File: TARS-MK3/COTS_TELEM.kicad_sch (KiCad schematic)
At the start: 13 parts, among them U1 RFM69HCW, U2 74HC4050D, U3 AP2112K-3.3, X1 uFL/SMA

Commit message: minor cots telem fixups
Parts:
- removed JP1: Conn_01x05_Female, symbol Connector:Conn_01x05_Female
- removed JP3: Conn_01x09_Female, symbol Connector:Conn_01x09_Female
- removed R2, R3: 100K, symbol D24V50F5:R
- removed U1: RFM69HCW, RF_Module:HOPERF_RFM9XW_THT, symbol RF_Module:RFM69HCW
- added J?: Conn_01x05_Male, Connector_PinHeader_2.54mm:PinHeader_1x05_P2.54mm_Vertical, symbol Connector:Conn_01x05_Male
- added J?: Conn_01x08_Male, Connector_PinHeader_2.54mm:PinHeader_1x09_P2.54mm_Vertical, symbol Connector:Conn_01x08_Male
- added U?: RFM96W-433S2, symbol RF_Module:RFM96W-433S2
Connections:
- net +3V3: no longer C1.1
- net GND: now also J?.7 (Pin_7), U?.1 (GND), U?.10 (GND), U?.8 (GND)
- net at JP2.1 (Pin_1), X1.ANTENNA (ANT): now also U?.9 (ANT)
- new net: J?.3 (Pin_3), U?.11 (DIO3)
- new net: J?.4 (Pin_4), U?.12 (DIO4)
- new net: J?.1 (Pin_1), U?.15 (DIO1)
- new net: J?.2 (Pin_2), U?.16 (DIO2)
- new net: J?.5 (Pin_5), U?.7 (DIO5)
- new net 3V3: C1.1, J?.8 (Pin_8), U?.13 (3.3V)
- new net B2B_SPI_MISO: J?.4 (Pin_4), U?.2 (MISO)
- new net B2B_SPI_MOSI: J?.5 (Pin_5), U?.3 (MOSI)
- new net B2B_SPI_SCK: J?.6 (Pin_6), U?.4 (SCK)
- new net TELEM_CS: J?.3 (Pin_3), U?.5 (NSS)
- new net TELEM_IRQ: J?.2 (Pin_2), U?.14 (DIO0)
- new net TELEM_RST: J?.1 (Pin_1), U?.6 (RESET)
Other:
- note removed: "DIO0"
- note removed: "DIO1"
- note removed: "DIO2"
- note removed: "DIO3"
- note removed: "DIO4"
- note removed: "DIO5"
- note removed: "MISO_3V"
- note removed: "MISO_5V"
- moved on the sheet: C1, C2, C3, JP2, R1, U2, U3, X1

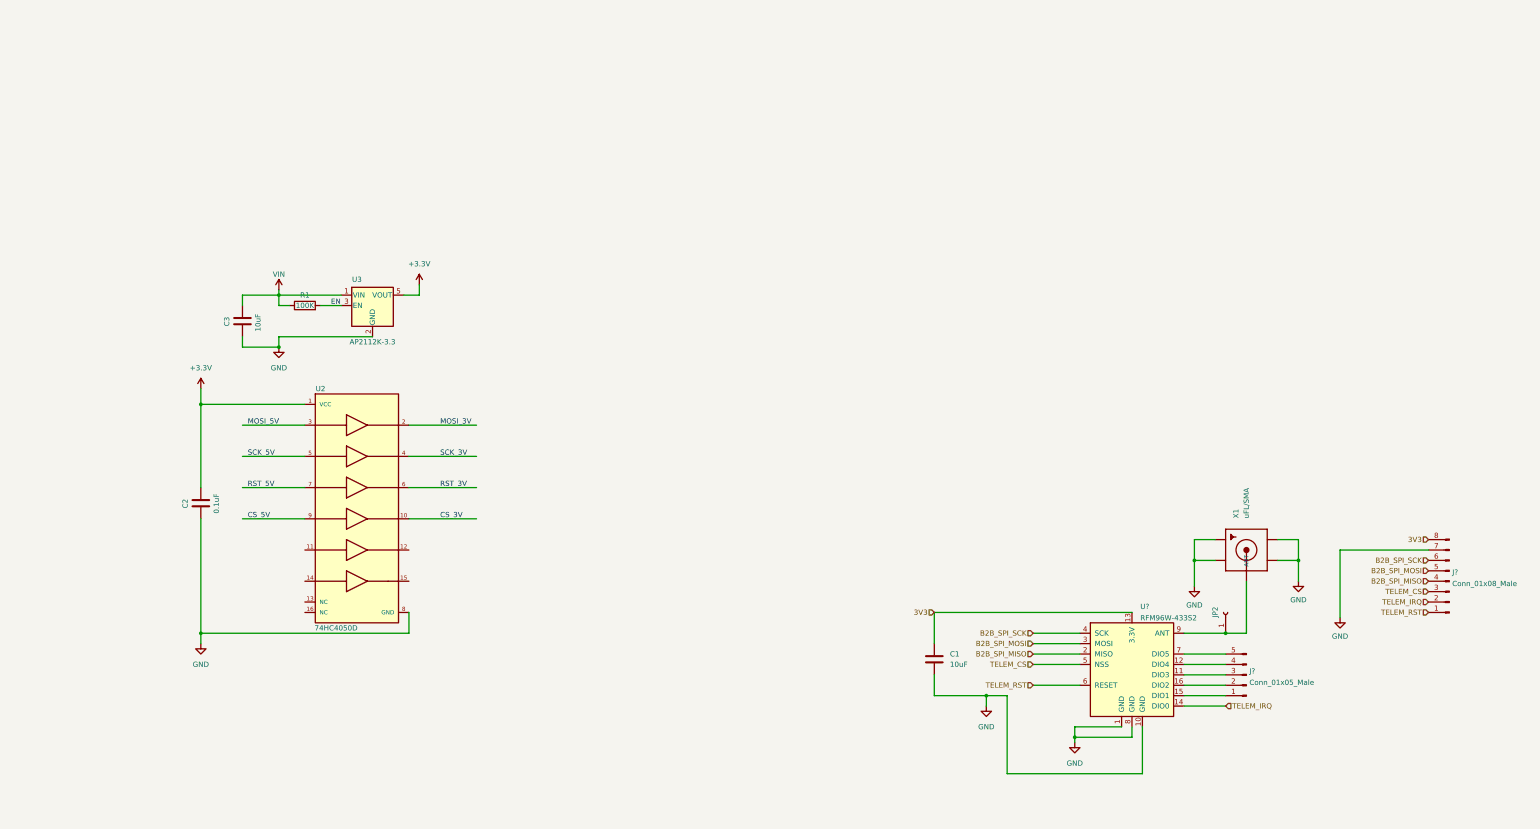
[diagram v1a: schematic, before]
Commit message: Applied template to COTS_TELEM
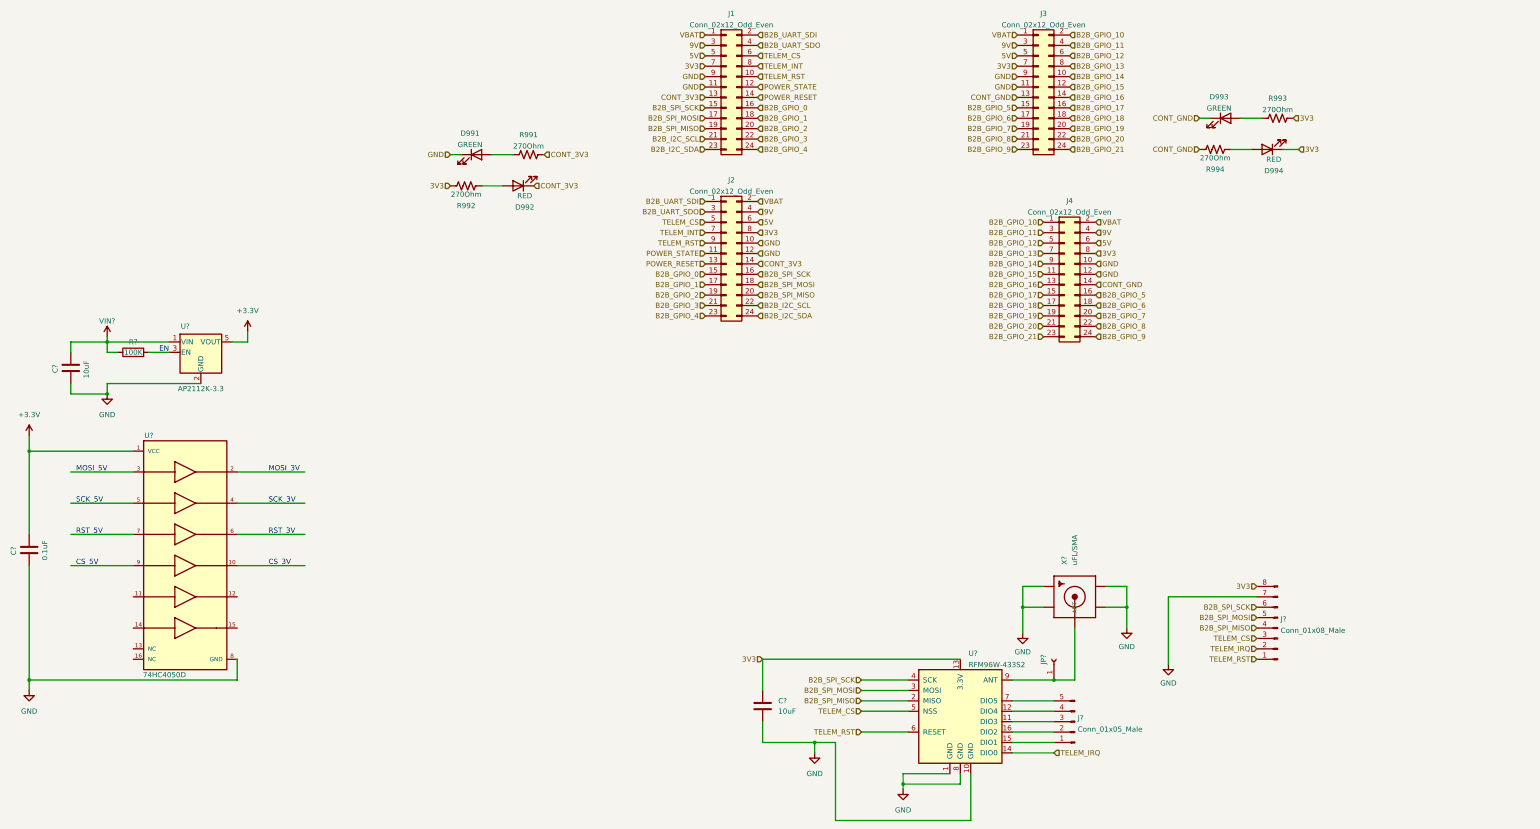
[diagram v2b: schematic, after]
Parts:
- removed C1, C3: 10uF, symbol D24V50F5:C
- removed C2: 0.1uF, symbol D24V50F5:C
- removed J?: Conn_01x05_Male, Connector_PinHeader_2.54mm:PinHeader_1x05_P2.54mm_Vertical, symbol Connector:Conn_01x05_Male
- removed J?: Conn_01x08_Male, Connector_PinHeader_2.54mm:PinHeader_1x09_P2.54mm_Vertical, symbol Connector:Conn_01x08_Male
- removed JP2: Conn_01x01_Female, symbol Connector:Conn_01x01_Female
- removed R1: 100K, symbol D24V50F5:R
- removed U2: 74HC4050D, Nexperia-SOT109-1-10_2018-0-*, symbol eec:74HC4050D,653
- removed U3: AP2112K-3.3, Package_TO_SOT_SMD:SOT-23-5, symbol Regulator_Linear:AP2112K-3.3
- removed U?: RFM96W-433S2, symbol RF_Module:RFM96W-433S2
- removed X1: uFL/SMA, symbol SENSOR_SUITE-rescue:SMACONNECTOR-SMACONNECTOR-SENSOR_SUITE-rescue
- added C? (x2): 10uF, symbol D24V50F5:C
- added C?: 0.1uF, symbol D24V50F5:C
- added D991, D993: GREEN, LED_SMD:LED_0805_2012Metric, symbol D24V50F5:LED
- added D992, D994: RED, LED_SMD:LED_0805_2012Metric, symbol D24V50F5:LED
- added J1, J2, J3, J4: Conn_02x12_Odd_Even, Connector_PinHeader_2.54mm:PinHeader_2x12_P2.54mm_Vertical_SMD, symbol Connector_Generic:Conn_02x12_Odd_Even
- added J?: Conn_01x05_Male, Connector_PinHeader_2.54mm:PinHeader_1x05_P2.54mm_Vertical, symbol Connector:Conn_01x05_Male
- added J?: Conn_01x08_Male, Connector_PinHeader_2.54mm:PinHeader_1x09_P2.54mm_Vertical, symbol Connector:Conn_01x08_Male
- added JP?: Conn_01x01_Female, symbol Connector:Conn_01x01_Female
- added R991, R992, R993, R994: 270Ohm, Resistor_SMD:R_0805_2012Metric, symbol D24V50F5:R_US
- added R?: 100K, symbol D24V50F5:R
- added U?: 74HC4050D, Nexperia-SOT109-1-10_2018-0-*, symbol eec:74HC4050D,653
- added U?: AP2112K-3.3, Package_TO_SOT_SMD:SOT-23-5, symbol Regulator_Linear:AP2112K-3.3
- added U?: RFM96W-433S2, symbol RF_Module:RFM96W-433S2
- added X?: uFL/SMA, symbol SENSOR_SUITE-rescue:SMACONNECTOR-SMACONNECTOR-SENSOR_SUITE-rescue
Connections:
- net +3V3: now also C?.1, U?.1 (VCC), U?.5 (VOUT)
- net 3V3: now also C?.1, D994.1 (K), J1.7 (Pin_7), J2.8 (Pin_8), J3.7 (Pin_7), J4.8 (Pin_8), J?.8 (Pin_8), R992.2, R993.2, U?.13 (3.3V)
- net B2B_SPI_MISO: now also J1.19 (Pin_19), J2.20 (Pin_20), J?.4 (Pin_4), U?.2 (MISO)
- net B2B_SPI_MOSI: now also J1.17 (Pin_17), J2.18 (Pin_18), J?.5 (Pin_5), U?.3 (MOSI)
- net B2B_SPI_SCK: now also J1.15 (Pin_15), J2.16 (Pin_16), J?.6 (Pin_6), U?.4 (SCK)
- net GND: now also C?.2, C?.2, C?.2, D991.1 (K), J1.11 (Pin_11), J1.9 (Pin_9), J2.10 (Pin_10), J2.12 (Pin_12), J3.11 (Pin_11), J3.9 (Pin_9), J4.10 (Pin_10), J4.12 (Pin_12), J?.7 (Pin_7), U?.1 (GND), U?.10 (GND), U?.2 (GND), U?.8 (GND), U?.8 (GND), X?.GND1, X?.GND2, X?.GND3, X?.GND4
- net TELEM_CS: now also J1.6 (Pin_6), J2.5 (Pin_5), J?.3 (Pin_3), U?.5 (NSS)
- net TELEM_IRQ: now also J?.2 (Pin_2), U?.14 (DIO0)
- net TELEM_RST: now also J1.10 (Pin_10), J2.9 (Pin_9), J?.1 (Pin_1), U?.6 (RESET)
- net VCC: now also C?.1, R?.1, U?.1 (VIN)
- new net: JP?.1 (Pin_1), U?.9 (ANT), X?.ANTENNA (ANT)
- new net: D992.2 (A), R992.1
- new net: D994.2 (A), R994.1
- new net: R?.2, U?.3 (EN)
- new net: D993.2 (A), R993.1
- new net: J?.1 (Pin_1), U?.15 (DIO1)
- new net: J?.2 (Pin_2), U?.16 (DIO2)
- new net: J?.3 (Pin_3), U?.11 (DIO3)
- new net: J?.4 (Pin_4), U?.12 (DIO4)
- new net: J?.5 (Pin_5), U?.7 (DIO5)
- new net: D991.2 (A), R991.1
- new net 5V: J1.5 (Pin_5), J2.6 (Pin_6), J3.5 (Pin_5), J4.6 (Pin_6)
- new net 9V: J1.3 (Pin_3), J2.4 (Pin_4), J3.3 (Pin_3), J4.4 (Pin_4)
- new net B2B_GPIO_0: J1.16 (Pin_16), J2.15 (Pin_15)
- new net B2B_GPIO_1: J1.18 (Pin_18), J2.17 (Pin_17)
- new net B2B_GPIO_10: J3.2 (Pin_2), J4.1 (Pin_1)
- new net B2B_GPIO_11: J3.4 (Pin_4), J4.3 (Pin_3)
- new net B2B_GPIO_12: J3.6 (Pin_6), J4.5 (Pin_5)
- new net B2B_GPIO_13: J3.8 (Pin_8), J4.7 (Pin_7)
- new net B2B_GPIO_14: J3.10 (Pin_10), J4.9 (Pin_9)
- new net B2B_GPIO_15: J3.12 (Pin_12), J4.11 (Pin_11)
- new net B2B_GPIO_16: J3.14 (Pin_14), J4.13 (Pin_13)
- new net B2B_GPIO_17: J3.16 (Pin_16), J4.15 (Pin_15)
- new net B2B_GPIO_18: J3.18 (Pin_18), J4.17 (Pin_17)
- new net B2B_GPIO_19: J3.20 (Pin_20), J4.19 (Pin_19)
- new net B2B_GPIO_2: J1.20 (Pin_20), J2.19 (Pin_19)
- new net B2B_GPIO_20: J3.22 (Pin_22), J4.21 (Pin_21)
- new net B2B_GPIO_21: J3.24 (Pin_24), J4.23 (Pin_23)
- new net B2B_GPIO_3: J1.22 (Pin_22), J2.21 (Pin_21)
- new net B2B_GPIO_4: J1.24 (Pin_24), J2.23 (Pin_23)
- new net B2B_GPIO_5: J3.15 (Pin_15), J4.16 (Pin_16)
- new net B2B_GPIO_6: J3.17 (Pin_17), J4.18 (Pin_18)
- new net B2B_GPIO_7: J3.19 (Pin_19), J4.20 (Pin_20)
- new net B2B_GPIO_8: J3.21 (Pin_21), J4.22 (Pin_22)
- new net B2B_GPIO_9: J3.23 (Pin_23), J4.24 (Pin_24)
- new net B2B_I2C_SCL: J1.21 (Pin_21), J2.22 (Pin_22)
- new net B2B_I2C_SDA: J1.23 (Pin_23), J2.24 (Pin_24)
- new net B2B_UART_SDI: J1.2 (Pin_2), J2.1 (Pin_1)
- new net B2B_UART_SDO: J1.4 (Pin_4), J2.3 (Pin_3)
- new net CONT_3V3: D992.1 (K), J1.13 (Pin_13), J2.14 (Pin_14), R991.2
- new net CONT_GND: D993.1 (K), J3.13 (Pin_13), J4.14 (Pin_14), R994.2
- new net POWER_RESET: J1.14 (Pin_14), J2.13 (Pin_13)
- new net POWER_STATE: J1.12 (Pin_12), J2.11 (Pin_11)
- new net TELEM_INT: J1.8 (Pin_8), J2.7 (Pin_7)
- new net VBAT: J1.1 (Pin_1), J2.2 (Pin_2), J3.1 (Pin_1), J4.2 (Pin_2)

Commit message: Finished COTS_TELEM PCB
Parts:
- removed C?: 10uF, symbol D24V50F5:C
- removed C?: 0.1uF, symbol D24V50F5:C
- removed J?: Conn_01x08_Male, Connector_PinHeader_2.54mm:PinHeader_1x09_P2.54mm_Vertical, symbol Connector:Conn_01x08_Male
- removed R?: 100K, symbol D24V50F5:R
- removed U?: 74HC4050D, Nexperia-SOT109-1-10_2018-0-*, symbol eec:74HC4050D,653
- removed U?: AP2112K-3.3, Package_TO_SOT_SMD:SOT-23-5, symbol Regulator_Linear:AP2112K-3.3
- C1: renamed from C?; footprint (none) -> Capacitor_SMD:C_0805_2012Metric
- JP1: renamed from JP?; footprint (none) -> TestPoint:TestPoint_Pad_D1.0mm
- U1: renamed from U?; footprint (none) -> RF_Module:HOPERF_RFM9XW_SMD
- X1: renamed from X?; footprint (none) -> uFL:uFL
- gave numbers to parts that had none: 1
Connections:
- net TELEM_IRQ is gone; now on net TELEM_INT: U1.14 (DIO0)
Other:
- note removed: "CS_3V"
- note removed: "CS_5V"
- note removed: "EN"
- note removed: "MOSI_3V"
- note removed: "MOSI_5V"
- note removed: "RST_3V"
- note removed: "RST_5V"
- note removed: "SCK_3V"
- note removed: "SCK_5V"

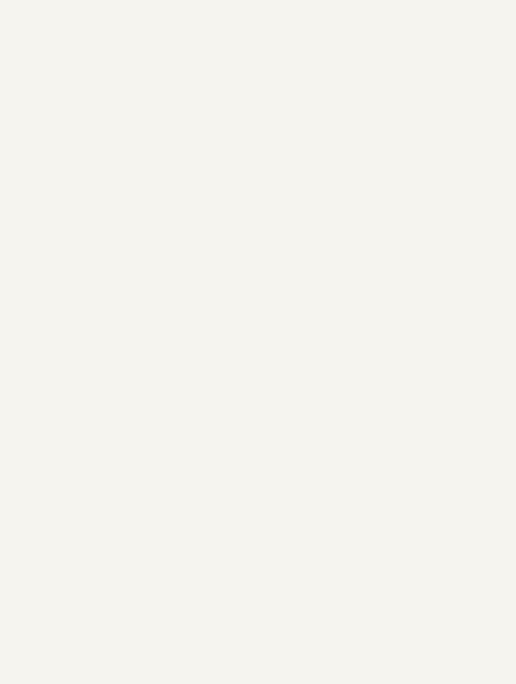
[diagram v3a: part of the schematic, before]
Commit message: added feather
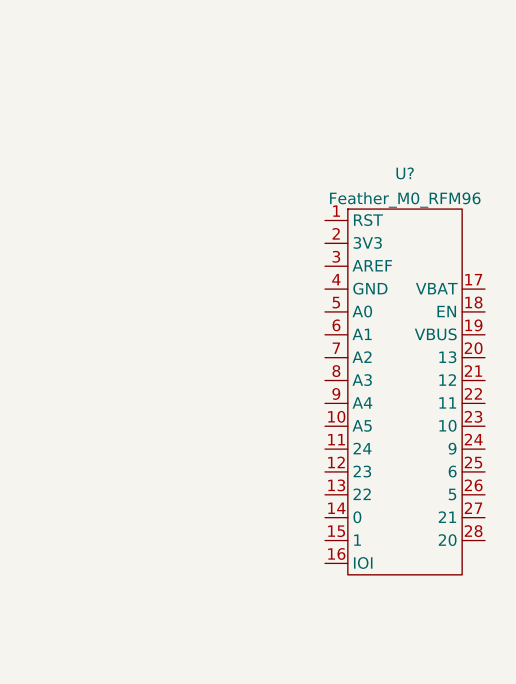
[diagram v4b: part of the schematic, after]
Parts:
- added U?: Feather_M0_RFM96, Feather:feather-m0-RFM69, symbol Feather:Feather_M0_RFM96

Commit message: minor tweaks
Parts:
- U2: renamed from U?; now left out of the parts list
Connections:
- net 3V3: now also U2.2 (3V3)
- net B2B_SPI_MISO: now also U2.13 (22)
- net B2B_SPI_MOSI: now also U2.12 (23)
- net B2B_SPI_SCK: now also U2.11 (24)
- net GND: now also U2.16 (IOI), U2.4 (GND)
- net TELEM_CS: now also U2.10 (A5)
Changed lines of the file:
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@@
     (stroke (width 0) (type default) (color 0 0 0 0))
   )
+  (hierarchical_label "B2B_SPI_MOSI" (shape input) (at 198.12 93.98 180)
+    (effects (font (size 1.27 1.27)) (justify right))
+  )
   (hierarchical_label "B2B_GPIO_11" (shape input) (at 120.65 -27.94 180)
     (effects (font (size 1.27 1.27)) (justify right))
@@
     (effects (font (size 1.27 1.27)) (justify left))
   )
+  (hierarchical_label "TELEM_CS" (shape input) (at 198.12 88.9 180)
+    (effects (font (size 1.27 1.27)) (justify right))
+  )
   (hierarchical_label "9V" (shape input) (at 133.35 -27.94 0)
     (effects (font (size 1.27 1.27)) (justify left))
@@
     (effects (font (size 1.27 1.27)) (justify left))
   )
+  (hierarchical_label "GND" (shape input) (at 198.12 73.66 180)
+    (effects (font (size 1.27 1.27)) (justify right))
+  )
   (hierarchical_label "9V" (shape input) (at 38.1 -73.66 180)
     (effects (font (size 1.27 1.27)) (justify right))
@@
     (effects (font (size 1.27 1.27)) (justify left))
   )
+  (hierarchical_label "3V3" (shape input) (at 198.12 68.58 180)
+    (effects (font (size 1.27 1.27)) (justify right))
+  )
   (hierarchical_label "B2B_GPIO_17" (shape input) (at 127 -58.42 0)
     (effects (font (size 1.27 1.27)) (justify left))
@@
     (effects (font (size 1.27 1.27)) (justify left))
   )
+  (hierarchical_label "B2B_SPI_SCK" (shape input) (at 198.12 91.44 180)
+    (effects (font (size 1.27 1.27)) (justify right))
+  )
+  (hierarchical_label "GND" (shape input) (at 198.12 104.14 180)
+    (effects (font (size 1.27 1.27)) (justify right))
+  )
   (hierarchical_label "B2B_GPIO_12" (shape input) (at 120.65 -25.4 180)
     (effects (font (size 1.27 1.27)) (justify right))
@@
   )
   (hierarchical_label "B2B_UART_SDO" (shape input) (at 38.1 -33.02 180)
+    (effects (font (size 1.27 1.27)) (justify right))
+  )
+  (hierarchical_label "B2B_SPI_MISO" (shape input) (at 198.12 96.52 180)
     (effects (font (size 1.27 1.27)) (justify right))
   )
@@
   )
   (symbol (lib_id "Feather:Feather_M0_RFM96") (at 207.01 85.09 0) (unit 1)
-    (in_bom yes) (on_board yes) (fields_autoplaced)
-    (property "Reference" "U?" (id 0) (at 207.01 60.8543 0))
+    (in_bom no) (on_board no) (fields_autoplaced)
+    (property "Reference" "U2" (id 0) (at 207.01 60.8543 0))
     (property "Value" "Feather_M0_RFM96" (id 1) (at 207.01 63.6294 0))
     (property "Footprint" "Feather:feather-m0-RFM69" (id 2) (at 207.01 104.14 0)
@@
     )
     (path "/180c5448-3d3e-49f1-b655-4a64a70b336b"
-      (reference "U?") (unit 1) (value "Feather_M0_RFM96") (footprint "Feather:feather-m0-RFM69")
+      (reference "U2") (unit 1) (value "Feather_M0_RFM96") (footprint "Feather:feather-m0-RFM69")
     )
     (path "/0a2ab516-8c00-42e4-a6c3-7c1326be2fa4"
